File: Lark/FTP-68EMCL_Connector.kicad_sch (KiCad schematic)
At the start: 6 parts, among them J4 B34B-PHDSS

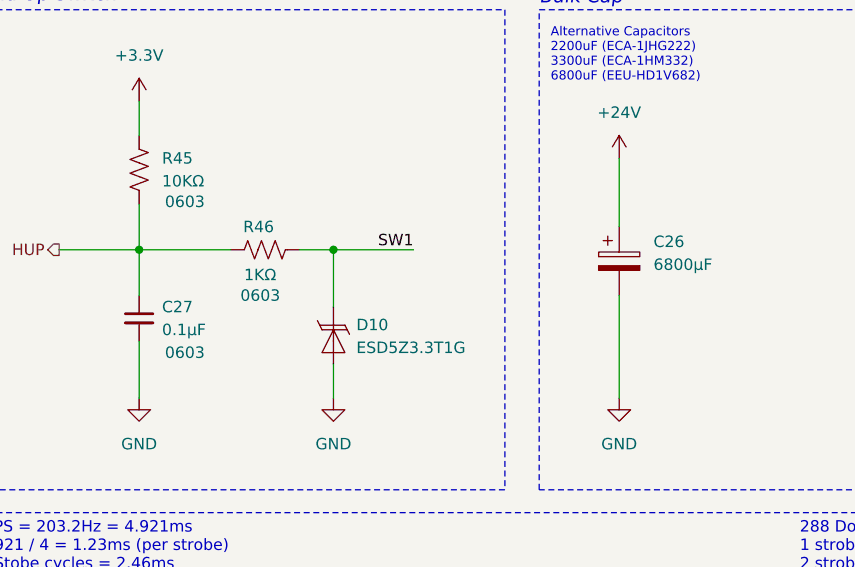
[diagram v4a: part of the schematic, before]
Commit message: updated WIP
- fixed high-side switch (swapped out pfets)
- swapped out bleeder fet.
- changed a few footprints.
- changed zeners to 15v ones
- added soft-start cap back in to the high-side switch.

(today ive mainly been struggling with the inrush current, but I think its solved now)
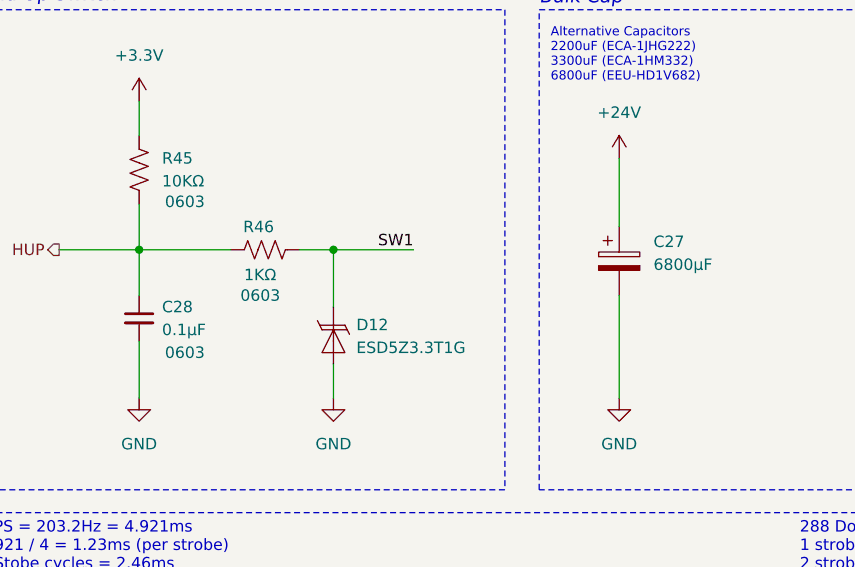
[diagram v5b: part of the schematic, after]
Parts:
- renumbered C26 to C27, C27 to C28, D10 to D12
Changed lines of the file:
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@@
 		(dnp no)
 		(fields_autoplaced yes)
-		(property "Reference" "#PWR0113"
+		(property "Reference" "#PWR0114"
 			(at 185.42 31.75 0)
 			(effects
@@
 			(project "Lark"
 				(path "/a351af57-4353-47da-9f45-7393de572768/6e291d34-e508-4d3b-a2e9-20acfef2b928"
-					(reference "#PWR0113")
+					(reference "#PWR0114")
 					(unit 1)
 				)
@@
 		(on_board yes)
 		(dnp no)
-		(property "Reference" "C27"
+		(property "Reference" "C28"
 			(at 38.1 134.6262 0)
 			(effects
@@
 			(project "Lark"
 				(path "/a351af57-4353-47da-9f45-7393de572768/6e291d34-e508-4d3b-a2e9-20acfef2b928"
-					(reference "C27")
+					(reference "C28")
 					(unit 1)
 				)
@@
 		(dnp no)
 		(fields_autoplaced yes)
-		(property "Reference" "#PWR0114"
+		(property "Reference" "#PWR0115"
 			(at 210.82 31.75 0)
 			(effects
@@
 			(project "Lark"
 				(path "/a351af57-4353-47da-9f45-7393de572768/6e291d34-e508-4d3b-a2e9-20acfef2b928"
-					(reference "#PWR0114")
+					(reference "#PWR0115")
 					(unit 1)
 				)
@@
 		(dnp no)
 		(fields_autoplaced yes)
-		(property "Reference" "#PWR0118"
+		(property "Reference" "#PWR0119"
 			(at 208.28 93.98 0)
 			(effects
@@
 			(project "Lark"
 				(path "/a351af57-4353-47da-9f45-7393de572768/6e291d34-e508-4d3b-a2e9-20acfef2b928"
-					(reference "#PWR0118")
+					(reference "#PWR0119")
 					(unit 1)
 				)
@@
 		(dnp no)
 		(fields_autoplaced yes)
-		(property "Reference" "#PWR0117"
+		(property "Reference" "#PWR0118"
 			(at 187.96 93.98 0)
 			(effects
@@
 			(project "Lark"
 				(path "/a351af57-4353-47da-9f45-7393de572768/6e291d34-e508-4d3b-a2e9-20acfef2b928"
-					(reference "#PWR0117")
+					(reference "#PWR0118")
 					(unit 1)
 				)
@@
 		(dnp no)
 		(fields_autoplaced yes)
-		(property "Reference" "#PWR0120"
+		(property "Reference" "#PWR0121"
 			(at 88.9 121.92 0)
 			(effects
@@
 			(project "Lark"
 				(path "/a351af57-4353-47da-9f45-7393de572768/6e291d34-e508-4d3b-a2e9-20acfef2b928"
-					(reference "#PWR0120")
+					(reference "#PWR0121")
 					(unit 1)
 				)
@@
 		(dnp no)
 		(fields_autoplaced yes)
-		(property "Reference" "#PWR0115"
+		(property "Reference" "#PWR0116"
 			(at 180.34 38.1 0)
 			(effects
@@
 			(project "Lark"
 				(path "/a351af57-4353-47da-9f45-7393de572768/6e291d34-e508-4d3b-a2e9-20acfef2b928"
-					(reference "#PWR0115")
+					(reference "#PWR0116")
 					(unit 1)
 				)
@@
 		(dnp no)
 		(fields_autoplaced yes)
-		(property "Reference" "#PWR0119"
+		(property "Reference" "#PWR0120"
 			(at 35.56 115.57 0)
 			(effects
@@
 			(project "Lark"
 				(path "/a351af57-4353-47da-9f45-7393de572768/6e291d34-e508-4d3b-a2e9-20acfef2b928"
-					(reference "#PWR0119")
+					(reference "#PWR0120")
 					(unit 1)
 				)
@@
 		(dnp no)
 		(fields_autoplaced yes)
-		(property "Reference" "C26"
+		(property "Reference" "C27"
 			(at 92.71 127.3809 0)
 			(effects
@@
 			(project ""
 				(path "/a351af57-4353-47da-9f45-7393de572768/6e291d34-e508-4d3b-a2e9-20acfef2b928"
-					(reference "C26")
+					(reference "C27")
 					(unit 1)
 				)
@@
 		(dnp no)
 		(fields_autoplaced yes)
-		(property "Reference" "D10"
+		(property "Reference" "D12"
 			(at 59.69 136.6201 90)
 			(effects
@@
 			(project "Lark"
 				(path "/a351af57-4353-47da-9f45-7393de572768/6e291d34-e508-4d3b-a2e9-20acfef2b928"
-					(reference "D10")
+					(reference "D12")
 					(unit 1)
 				)
@@
 		(dnp no)
 		(fields_autoplaced yes)
-		(property "Reference" "#PWR0116"
+		(property "Reference" "#PWR0117"
 			(at 215.9 38.1 0)
 			(effects
@@
 			(project "Lark"
 				(path "/a351af57-4353-47da-9f45-7393de572768/6e291d34-e508-4d3b-a2e9-20acfef2b928"
-					(reference "#PWR0116")
+					(reference "#PWR0117")
 					(unit 1)
 				)
@@
 		(dnp no)
 		(fields_autoplaced yes)
-		(property "Reference" "#PWR0122"
+		(property "Reference" "#PWR0123"
 			(at 57.15 151.13 0)
 			(effects
@@
 			(project "Lark"
 				(path "/a351af57-4353-47da-9f45-7393de572768/6e291d34-e508-4d3b-a2e9-20acfef2b928"
-					(reference "#PWR0122")
+					(reference "#PWR0123")
 					(unit 1)
 				)
@@
 		(dnp no)
 		(fields_autoplaced yes)
-		(property "Reference" "#PWR0121"
+		(property "Reference" "#PWR0122"
 			(at 35.56 151.13 0)
 			(effects
@@
 			(project "Lark"
 				(path "/a351af57-4353-47da-9f45-7393de572768/6e291d34-e508-4d3b-a2e9-20acfef2b928"
-					(reference "#PWR0121")
+					(reference "#PWR0122")
 					(unit 1)
 				)
@@
 		(dnp no)
 		(fields_autoplaced yes)
-		(property "Reference" "#PWR0123"
+		(property "Reference" "#PWR0124"
 			(at 88.9 151.13 0)
 			(effects
@@
 			(project "Lark"
 				(path "/a351af57-4353-47da-9f45-7393de572768/6e291d34-e508-4d3b-a2e9-20acfef2b928"
-					(reference "#PWR0123")
-					(unit 1)
-				)
+					(reference "#PWR0124")
+					(unit 1)
+				)

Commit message: started on layout, WIP
I'm not a fan of how its going, I feel like I might redo it, before I get to far into it. A patchy foundation makes an unstable house.
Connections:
- net SW is gone; now on net SW1: J4.21 (Pin_21)
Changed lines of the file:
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@@
+		)
+	)
+	(label "{slash}STROBE_1"
+		(at 104.14 30.48 180)
+		(effects
+			(font
+				(size 1.27 1.27)
+			)
+			(justify right bottom)
+		)
+	)
+	(label "{slash}STROBE_6"
+		(at 104.14 43.18 180)
+		(effects
+			(font
+				(size 1.27 1.27)
+			)
+			(justify right bottom)
 		)
 	)
@@
 		)
 	)
+	(label "{slash}STROBE_5"
+		(at 104.14 38.1 180)
+		(effects
+			(font
+				(size 1.27 1.27)
+			)
+			(justify right bottom)
+		)
+	)
+	(label "SW1"
+		(at 170.18 54.61 0)
+		(effects
+			(font
+				(size 1.27 1.27)
+			)
+			(justify left bottom)
+		)
+	)
+	(label "{slash}STROBE_4"
+		(at 104.14 40.64 180)
+		(effects
+			(font
+				(size 1.27 1.27)
+			)
+			(justify right bottom)
+		)
+	)
+	(label "{slash}STROBE_3"
+		(at 104.14 35.56 180)
+		(effects
+			(font
+				(size 1.27 1.27)
+			)
+			(justify right bottom)
+		)
+	)
+	(label "{slash}STROBE_1"
+		(at 170.18 64.77 0)
+		(effects
+			(font
+				(size 1.27 1.27)
+			)
+			(justify left bottom)
+		)
+	)
+	(label "DATA"
+		(at 104.14 45.72 180)
+		(effects
+			(font
+				(size 1.27 1.27)
+			)
+			(justify right bottom)
+		)
+	)
 	(label "{slash}LATCH"
 		(at 104.14 48.26 180)
@@
 		)
 	)
-	(label "{slash}STROBE_6"
-		(at 104.14 40.64 180)
-		(effects
-			(font
-				(size 1.27 1.27)
-			)
-			(justify right bottom)
-		)
-	)
-	(label "SW"
-		(at 170.18 54.61 0)
-		(effects
-			(font
-				(size 1.27 1.27)
-			)
-			(justify left bottom)
-		)
-	)
-	(label "DATA"
-		(at 104.14 43.18 180)
-		(effects
-			(font
-				(size 1.27 1.27)
-			)
-			(justify right bottom)
-		)
-	)
-	(label "{slash}STROBE_1"
-		(at 170.18 64.77 0)
-		(effects
-			(font
-				(size 1.27 1.27)
-			)
-			(justify left bottom)
-		)
-	)
-	(label "{slash}STROBE_2"
-		(at 104.14 30.48 180)
-		(effects
-			(font
-				(size 1.27 1.27)
-			)
-			(justify right bottom)
-		)
-	)
 	(label "{slash}STROBE_3"
 		(at 170.18 67.31 0)
@@
 		)
 	)
-	(label "{slash}STROBE_1"
+	(label "CLOCK"
 		(at 104.14 27.94 180)
 		(effects
@@
 		)
 	)
-	(label "CLOCK"
-		(at 104.14 45.72 180)
-		(effects
-			(font
-				(size 1.27 1.27)
-			)
-			(justify right bottom)
-		)
-	)
-	(label "{slash}STROBE_5"
-		(at 104.14 38.1 180)
-		(effects
-			(font
-				(size 1.27 1.27)
-			)
-			(justify right bottom)
-		)
-	)
 	(label "DATA"
 		(at 228.6 77.47 180)
@@
 		)
 	)
-	(label "{slash}STROBE_3"
-		(at 104.14 33.02 180)
-		(effects
-			(font
-				(size 1.27 1.27)
-			)
-			(justify right bottom)
-		)
-	)
 	(label "{slash}LATCH"
 		(at 228.6 59.69 180)
@@
 		)
 	)
+	(label "{slash}STROBE_2"
+		(at 104.14 33.02 180)
+		(effects
+			(font
+				(size 1.27 1.27)
+			)
+			(justify right bottom)
+		)
+	)
 	(label "{slash}STROBE_6"
 		(at 170.18 77.47 0)
@@
 		)
 	)
-	(label "{slash}STROBE_4"
-		(at 104.14 35.56 180)
-		(effects
-			(font
-				(size 1.27 1.27)
-			)
-			(justify right bottom)
+	(hierarchical_label "{slash}STB1"
+		(shape input)
+		(at 30.48 30.48 180)
+		(effects
+			(font
+				(size 1.27 1.27)
+			)
+			(justify right)
 		)
 	)
@@
 		)
 	)
+	(hierarchical_label "{slash}LAT"
+		(shape input)
+		(at 30.48 48.26 180)
+		(effects
+			(font
+				(size 1.27 1.27)
+			)
+			(justify right)
+		)
+	)
 	(hierarchical_label "{slash}OE"
 		(shape input)
 		(at 30.48 52.07 180)
+		(effects
+			(font
+				(size 1.27 1.27)
+			)
+			(justify right)
+		)
+	)
+	(hierarchical_label "DIN"
+		(shape input)
+		(at 30.48 45.72 180)
 		(effects
 			(font
@@
 		)
 	)
+	(hierarchical_label "{slash}STB6"
+		(shape input)
+		(at 30.48 43.18 180)
+		(effects
+			(font
+				(size 1.27 1.27)
+			)
+			(justify right)
+		)
+	)
+	(hierarchical_label "PHK_M"
+		(shape output)
+		(at 229.87 52.07 0)
+		(effects
+			(font
+				(size 1.27 1.27)
+			)
+			(justify left)
+		)
+	)
 	(hierarchical_label "{slash}STB2"
 		(shape input)
-		(at 30.48 30.48 180)
-		(effects
-			(font
-				(size 1.27 1.27)
-			)
-			(justify right)
-		)
-	)
-	(hierarchical_label "DIN"
-		(shape input)
-		(at 30.48 43.18 180)
-		(effects
-			(font
-				(size 1.27 1.27)
-			)
-			(justify right)
-		)
-	)
-	(hierarchical_label "{slash}STB3"
-		(shape input)
 		(at 30.48 33.02 180)
 		(effects
@@
 		)
 	)
-	(hierarchical_label "PHK_M"
-		(shape output)
-		(at 229.87 52.07 0)
-		(effects
-			(font
-				(size 1.27 1.27)
-			)
-			(justify left)
-		)
-	)
-	(hierarchical_label "CLK"
-		(shape input)
-		(at 30.48 45.72 180)
-		(effects
-			(font
-				(size 1.27 1.27)
-			)
-			(justify right)
-		)
-	)
-	(hierarchical_label "{slash}STB1"
-		(shape input)
-		(at 30.48 27.94 180)
-		(effects
-			(font
-				(size 1.27 1.27)
-			)
-			(justify right)
-		)
-	)
 	(hierarchical_label "PHE_P"
 		(shape output)
@@
 			)
 			(justify left)
-		)
-	)
-	(hierarchical_label "{slash}STB6"
-		(shape input)
-		(at 30.48 40.64 180)
-		(effects
-			(font
-				(size 1.27 1.27)
-			)
-			(justify right)
 		)
 	)
@@
 		)
 	)
-	(hierarchical_label "{slash}STB5"
-		(shape input)
-		(at 30.48 38.1 180)
+	(hierarchical_label "{slash}STB3"
+		(shape input)
+		(at 30.48 35.56 180)
+		(effects
+			(font
+				(size 1.27 1.27)
+			)
+			(justify right)
+		)
+	)
+	(hierarchical_label "{slash}STB4"
+		(shape input)
+		(at 30.48 40.64 180)
 		(effects
 			(font
@@
 		)
 	)
+	(hierarchical_label "CLK"
+		(shape input)
+		(at 30.48 27.94 180)
+		(effects
+			(font
+				(size 1.27 1.27)
+			)
+			(justify right)
+		)
+	)
 	(hierarchical_label "MTMP"
 		(shape output)
@@
 		)
 	)
-	(hierarchical_label "{slash}LAT"
-		(shape input)
-		(at 30.48 48.26 180)
-		(effects
-			(font
-				(size 1.27 1.27)
-			)
-			(justify right)
-		)
-	)
-	(hierarchical_label "{slash}STB4"
-		(shape input)
-		(at 30.48 35.56 180)
-		(effects
-			(font
+	(hierarchical_label "{slash}STB5"
+		(shape input)
+		(at 30.48 38.1 180)
+		(effects
+			(font
